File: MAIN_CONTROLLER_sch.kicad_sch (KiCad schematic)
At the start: 9 parts, among them U1 ESP32-S3-WROOM-1-N16R2

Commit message: Finished Last sheets
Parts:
- added R98: 10k, symbol Device:R
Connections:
- net GND: now also R98.1
- net IO3: now reaches U1.15 (IO3)
- net IO3: now also R98.2
- net LF_TMS3705_CE: no longer names the net of U1.6 (IO6)
- net RF_SW_B renamed TFT_BL_PWM
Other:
- moved on the sheet: C24

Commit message: finished annotation
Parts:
- renumbered C24 to C23, C22 to C24, C23 to C25, R21 to R20, R20 to R21, R98 to R23
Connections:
- net ESP_CONSOLE_TX_RAW: now reaches R22.1, U1.37 (TXD0)
- net IO3 renamed ESP_GPIO3_STRAP_PD
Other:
- title: (none) -> ESP32-S3 Main Controller and System Interfaces
- moved on the sheet: R22, R23
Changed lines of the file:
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@@
 	(generator_version "10.0")
 	(paper "A4")
+	(title_block
+		(title "ESP32-S3 Main Controller and System Interfaces")
+		(rev "A")
+	)
 	(rectangle
 		(start 13.97 81.28)
@@
 	(wire
 		(pts
-			(xy 139.7 119.38) (xy 142.24 119.38)
+			(xy 114.3 118.11) (xy 116.84 118.11)
 		)
 		(stroke
@@
 	(wire
 		(pts
-			(xy 149.86 119.38) (xy 154.94 119.38)
+			(xy 124.46 118.11) (xy 147.32 118.11)
 		)
 		(stroke
@@
 	(wire
 		(pts
-			(xy 231.14 74.93) (xy 236.22 74.93)
+			(xy 247.65 74.93) (xy 256.54 74.93)
 		)
 		(stroke
@@
 	(wire
 		(pts
-			(xy 213.36 74.93) (xy 223.52 74.93)
+			(xy 213.36 74.93) (xy 240.03 74.93)
 		)
 		(stroke
@@
 	(wire
 		(pts
-			(xy 139.7 121.92) (xy 139.7 119.38)
+			(xy 114.3 120.65) (xy 114.3 118.11)
 		)
 		(stroke
@@
 	(wire
 		(pts
-			(xy 163.83 87.63) (xy 182.88 87.63)
+			(xy 160.02 87.63) (xy 182.88 87.63)
 		)
 		(stroke
@@
 		)
 	)
-	(label "IO3"
-		(at 154.94 119.38 180)
+	(label "ESP_CONSOLE_TX_RAW"
+		(at 215.9 74.93 0)
+		(effects
+			(font
+				(size 1.27 1.27)
+			)
+			(justify left bottom)
+		)
+	)
+	(label "ESP_GPIO3_STRAP_PD"
+		(at 147.32 118.11 180)
 		(effects
 			(font
@@
 		)
 	)
-	(label "IO3"
-		(at 163.83 87.63 0)
+	(label "ESP_GPIO3_STRAP_PD"
+		(at 160.02 87.63 0)
 		(effects
 			(font
@@
 	(hierarchical_label "CONSOLE_TX"
 		(shape output)
-		(at 236.22 74.93 0)
+		(at 256.54 74.93 0)
 		(effects
 			(font
@@
 	(symbol
 		(lib_id "Device:R")
-		(at 146.05 119.38 90)
+		(at 120.65 118.11 90)
 		(unit 1)
 		(body_style 1)
@@
 		(dnp no)
 		(fields_autoplaced yes)
-		(property "Reference" "R98"
-			(at 146.05 113.03 90)
+		(property "Reference" "R23"
+			(at 120.65 111.76 90)
 			(show_name no)
 			(do_not_autoplace no)
@@
 		)
 		(property "Value" "10k"
-			(at 146.05 115.57 90)
+			(at 120.65 114.3 90)
 			(show_name no)
 			(do_not_autoplace no)
@@
 		)
 		(property "Footprint" ""
-			(at 146.05 121.158 90)
+			(at 120.65 119.888 90)
 			(hide yes)
 			(show_name no)
@@
 		)
 		(property "Datasheet" ""
-			(at 146.05 119.38 0)
+			(at 120.65 118.11 0)
 			(hide yes)
 			(show_name no)
@@
 		)
 		(property "Description" "Resistor"
-			(at 146.05 119.38 0)
+			(at 120.65 118.11 0)
 			(hide yes)
 			(show_name no)
@@
 			(project "FOBtool_HW"
 				(path "/4178b7d0-cf29-4cf2-b214-acbbbd97d338/911e9b50-e380-47e6-b4a6-ef60861d1588"
-					(reference "R98")
+					(reference "R23")
 					(unit 1)
 				)
@@
 		(dnp no)
 		(fields_autoplaced yes)
-		(property "Reference" "C24"
+		(property "Reference" "C23"
 			(at 142.24 62.2299 0)
 			(show_name no)
@@
 			(project "FOBtool_HW"
 				(path "/4178b7d0-cf29-4cf2-b214-acbbbd97d338/911e9b50-e380-47e6-b4a6-ef60861d1588"
-					(reference "C24")
+					(reference "C23")
 					(unit 1)
 				)
@@
 		(dnp no)
 		(fields_autoplaced yes)
-		(property "Reference" "R20"
+		(property "Reference" "R21"
 			(at 133.35 87.6299 0)
 			(show_name no)
@@
 			(project "FOBtool_HW"
 				(path "/4178b7d0-cf29-4cf2-b214-acbbbd97d338/911e9b50-e380-47e6-b4a6-ef60861d1588"
-					(reference "R20")
+					(reference "R21")
 					(unit 1)
 				)
@@
 	(symbol
 		(lib_id "Device:R")
-		(at 227.33 74.93 90)
+		(at 243.84 74.93 90)
 		(unit 1)
 		(body_style 1)
@@
 		(fields_autoplaced yes)
 		(property "Reference" "R22"
-			(at 227.33 68.58 90)
+			(at 243.84 68.58 90)
 			(show_name no)
 			(do_not_autoplace no)
@@
 		)
 		(property "Value" "499R"
-			(at 227.33 71.12 90)
+			(at 243.84 71.12 90)
 			(show_name no)
 			(do_not_autoplace no)
@@
 		)
 		(property "Footprint" ""
-			(at 227.33 76.708 90)
+			(at 243.84 76.708 90)
 			(hide yes)
 			(show_name no)
@@
 		)
 		(property "Datasheet" ""
-			(at 227.33 74.93 0)
+			(at 243.84 74.93 0)
 			(hide yes)
 			(show_name no)
@@
 		)
 		(property "Description" "Resistor"
-			(at 227.33 74.93 0)
+			(at 243.84 74.93 0)
 			(hide yes)
 			(show_name no)
@@
 		(dnp no)
 		(fields_autoplaced yes)
-		(property "Reference" "R21"
+		(property "Reference" "R20"
 			(at 124.46 87.6299 0)
 			(show_name no)
@@
 			(project "FOBtool_HW"
 				(path "/4178b7d0-cf29-4cf2-b214-acbbbd97d338/911e9b50-e380-47e6-b4a6-ef60861d1588"
-					(reference "R21")
+					(reference "R20")
 					(unit 1)
 				)
@@
 		(dnp no)
 		(fields_autoplaced yes)
-		(property "Reference" "C23"
+		(property "Reference" "C25"
 			(at 254 52.0699 0)
 			(show_name no)
@@
 			(project "FOBtool_HW"
 				(path "/4178b7d0-cf29-4cf2-b214-acbbbd97d338/911e9b50-e380-47e6-b4a6-ef60861d1588"
-					(reference "C23")
+					(reference "C25")
 					(unit 1)
 				)
@@
 		(dnp no)
 		(fields_autoplaced yes)
-		(property "Reference" "C22"
+		(property "Reference" "C24"
 			(at 227.33 52.0699 0)
 			(show_name no)
@@
 			(project "FOBtool_HW"
 				(path "/4178b7d0-cf29-4cf2-b214-acbbbd97d338/911e9b50-e380-47e6-b4a6-ef60861d1588"
-					(reference "C22")
+					(reference "C24")
 					(unit 1)
 				)
@@
 	(symbol
 		(lib_id "power:GND")
-		(at 139.7 121.92 0)
+		(at 114.3 120.65 0)
 		(unit 1)
 		(body_style 1)
@@
 		(fields_autoplaced yes)
 		(property "Reference" "#PWR0247"
-			(at 139.7 128.27 0)
+			(at 114.3 127 0)
 			(hide yes)
 			(show_name no)
@@
 		)
 		(property "Value" "GND"
-			(at 139.7 127 0)
+			(at 114.3 125.73 0)
 			(show_name no)
 			(do_not_autoplace no)
@@
 		)
 		(property "Footprint" ""
-			(at 139.7 121.92 0)
+			(at 114.3 120.65 0)
 			(hide yes)
 			(show_name no)
@@
 		)
 		(property "Datasheet" ""
-			(at 139.7 121.92 0)
+			(at 114.3 120.65 0)
 			(hide yes)
 			(show_name no)
@@
 		)
 		(property "Description" "Power symbol creates a global label with name \"GND\" , ground"
-			(at 139.7 121.92 0)
-			(hide yes)
-			(show_name no)
+			(at 114.3 120.65 0)
+			(hide yes)
+			(show_name no)

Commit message: finished ANCHOR_DOCK sheet
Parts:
- C23: footprint (none) -> Capacitor_SMD:C_0603_1608Metric; DISTRIBUTOR_LINK (none) -> https://www.mouser.com/ProductDetail/Murata-Electronics/GRM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; MANUFACTURER (none) -> Murata; MPN (none) -> GRM188R71C105KA12D; Notes (none) -> N/A
- C24: footprint (none) -> Capacitor_SMD:C_1206_3216Metric; DISTRIBUTOR_LINK (none) -> https://www.mouser.com/ProductDetail/Murata-Electronics/GRM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; MANUFACTURER (none) -> Murata; MPN (none) -> GRM31CR71A226KE15L; Notes (none) -> Verify effective capacitance under DC bias.
- C25: footprint (none) -> Capacitor_SMD:C_0603_1608Metric; DISTRIBUTOR_LINK (none) -> https://www.mouser.com/ProductDetail/Murata-Electronics/GRM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; MANUFACTURER (none) -> Murata; MPN (none) -> GRM188R71C104KA01D; Notes (none) -> N/A
- R18, R19, R23: footprint (none) -> Resistor_SMD:R_0603_1608Metric; DISTRIBUTOR_LINK (none) -> https://www.mouser.com/ProductDetail/YAGEO/RC0603FR-0710KL?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; MANUFACTURER (none) -> Yageo; MPN (none) -> RC0603FR-0710KL; Notes (none) -> N/A
- R20, R21: footprint (none) -> Resistor_SMD:R_0603_1608Metric; DISTRIBUTOR_LINK (none) -> https://www.mouser.com/ProductDetail/YAGEO/RC0603FR-072K2L?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; MANUFACTURER (none) -> Yageo; MPN (none) -> RC0603FR-072K2L; Notes (none) -> N/A
- R22: footprint (none) -> Resistor_SMD:R_0603_1608Metric; DISTRIBUTOR_LINK (none) -> https://www.mouser.com/ProductDetail/YAGEO/RC0603FR-07499RL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; MANUFACTURER (none) -> Yageo; MPN (none) -> RC0603FR-07499RL; Notes (none) -> N/A
- U1: DISTRIBUTOR_LINK (none) -> https://www.mouser.com/ProductDetail/Espressif-Systems/ESP3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; MANUFACTURER (none) -> Espressif; MPN (none) -> ESP32-S3-WROOM-1-N16R2; Notes (none) -> Keepout required under module antenna.

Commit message: the schematic is finished
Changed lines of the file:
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@@
 	(wire
 		(pts
-			(xy 160.02 87.63) (xy 182.88 87.63)
+			(xy 146.05 87.63) (xy 182.88 87.63)
 		)
 		(stroke
@@
 	)
 	(label "ESP_GPIO3_STRAP_PD"
-		(at 160.02 87.63 0)
+		(at 146.05 87.63 0)
 		(effects
 			(font

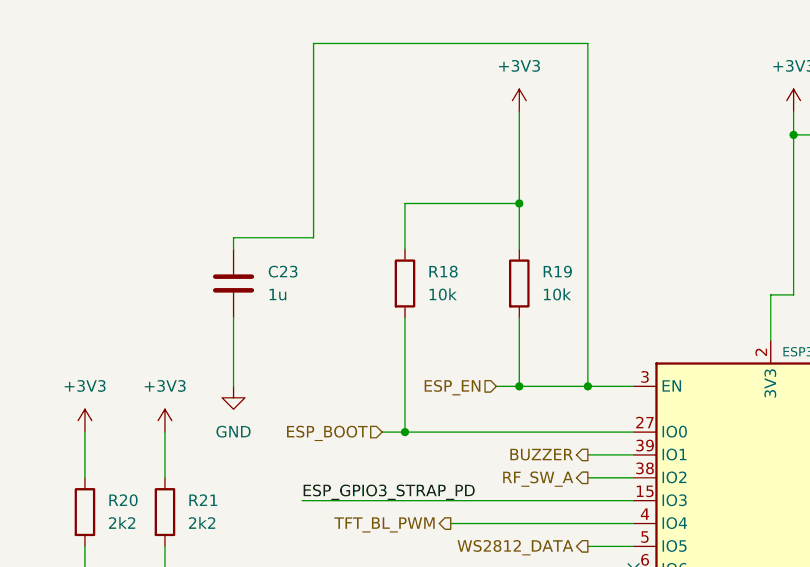
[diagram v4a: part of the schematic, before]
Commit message: changiong bootsel buttom in rp
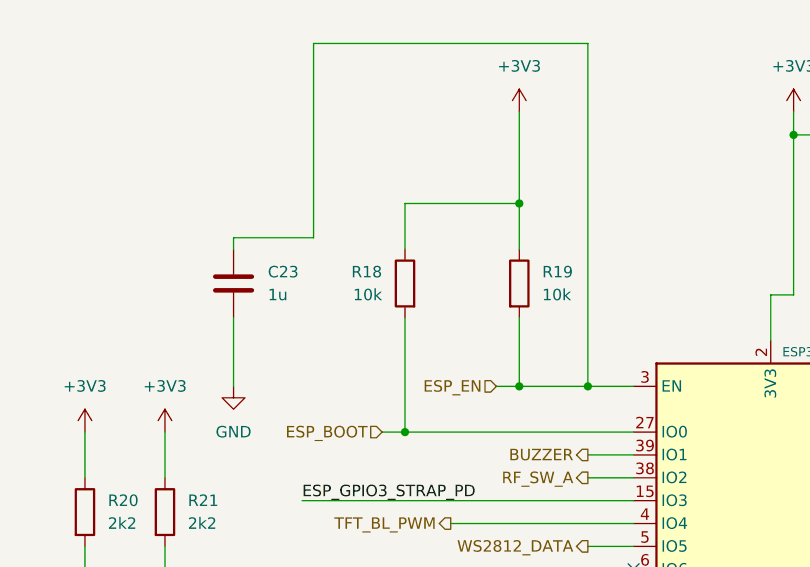
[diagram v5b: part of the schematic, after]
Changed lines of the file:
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@@
 	(wire
 		(pts
-			(xy 213.36 92.71) (xy 219.71 92.71)
-		)
-		(stroke
-			(width 0)
-			(type default)
-		)
-	)
-	(wire
-		(pts
 			(xy 152.4 101.6) (xy 152.4 102.87)
 		)
@@
 	(wire
 		(pts
+			(xy 213.36 92.71) (xy 219.71 92.71)
+		)
+		(stroke
+			(width 0)
+			(type default)
+		)
+	)
+	(wire
+		(pts
 			(xy 157.48 67.31) (xy 157.48 80.01)
 		)
@@
 		(lib_id "Device:R")
 		(at 157.48 63.5 0)
+		(mirror y)
 		(unit 1)
 		(body_style 1)
@@
 		(in_pos_files yes)
 		(dnp no)
-		(fields_autoplaced yes)
 		(property "Reference" "R18"
-			(at 160.02 62.2299 0)
+			(at 154.94 62.2299 0)
 			(show_name no)
 			(do_not_autoplace no)
@@
 		)
 		(property "Value" "10k"
-			(at 160.02 64.7699 0)
+			(at 154.94 64.7699 0)
 			(show_name no)
 			(do_not_autoplace no)
@@
 		)
 		(property "Footprint" "Resistor_SMD:R_0603_1608Metric"
-			(at 155.702 63.5 90)
+			(at 159.258 63.5 90)
 			(hide yes)
 			(show_name no)
